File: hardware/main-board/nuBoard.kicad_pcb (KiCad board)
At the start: 6 copper layers, 141.7 x 105.1 mm, 343 parts, among them J1 FPGA Debug, J2 Barrel_Jack_Switch, J3 USB_C_Receptacle_USB2.0_16P, J4 MCU Debug, J5 Conn_01x34_Socket, J6 Conn_01x34_Socket, J7 Conn_01x34_Socket, J8 Conn_01x34_Socket, Q1 NVF5P03T3G, Q2 BSR802NL6327, SW1 MCU_Reset, SW2 MCU_Boot, U1 T120F484, U10 W25Q128JVS, U11 RP2040, U2 IS66WVH8M8BLL-100B1LI, U24 SN74LVC8T245PWR, U25 SN74LVC8T245PWR, U26 SN74LVC8T245PWR, U27 SN74LVC8T245PWR, U28 SN74LVC8T245PWR, U29 SN74LVC8T245PWR, U3 TPS2116DRL, U30 SN74LVC8T245PWR, U31 SN74LVC8T245PWR, U32 SN74LVC8T245PWR, U33 SN74LVC8T245PWR, U34 SN74LVC8T245PWR, U35 SN74LVC8T245PWR, U36 TXS0108EPW, U37 SN74LVC1T45DRL, U38 SN74LVC1T45DRL, U39 SN74LVC1T45DRL, U4 AP2112K-3.3, U40 SN74LVC1T45DRL, U41 TXS0108EPW, U5 AP2112K-3.3, U6 TPS563201, U7 TPS563201, U8 UCC27524D, U9 TPS2111APWR, Y1 50Mhz, Y2 12Mhz

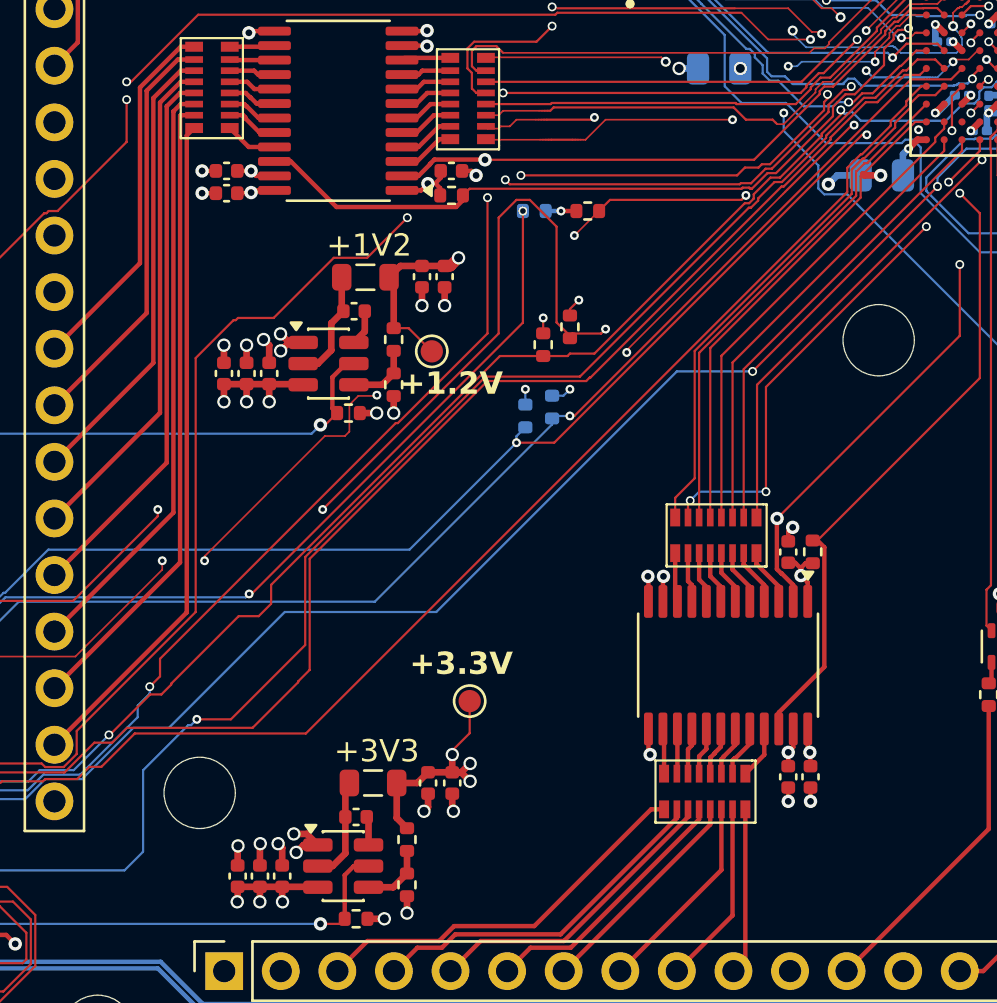
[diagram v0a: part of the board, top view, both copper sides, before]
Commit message: Fit power inductors for the FPGA buck converters
L1 and L2 used C16903, a ferrite bead, which made U6 and U7 whine and
damaged U6. Switch to C964122 in a 1008 footprint. Note that the
HyperRAM is held deselected until it is supported.

Claude-Session: https://claude.ai/code/session_01Mb721YdebqpSQrfvW2MyND
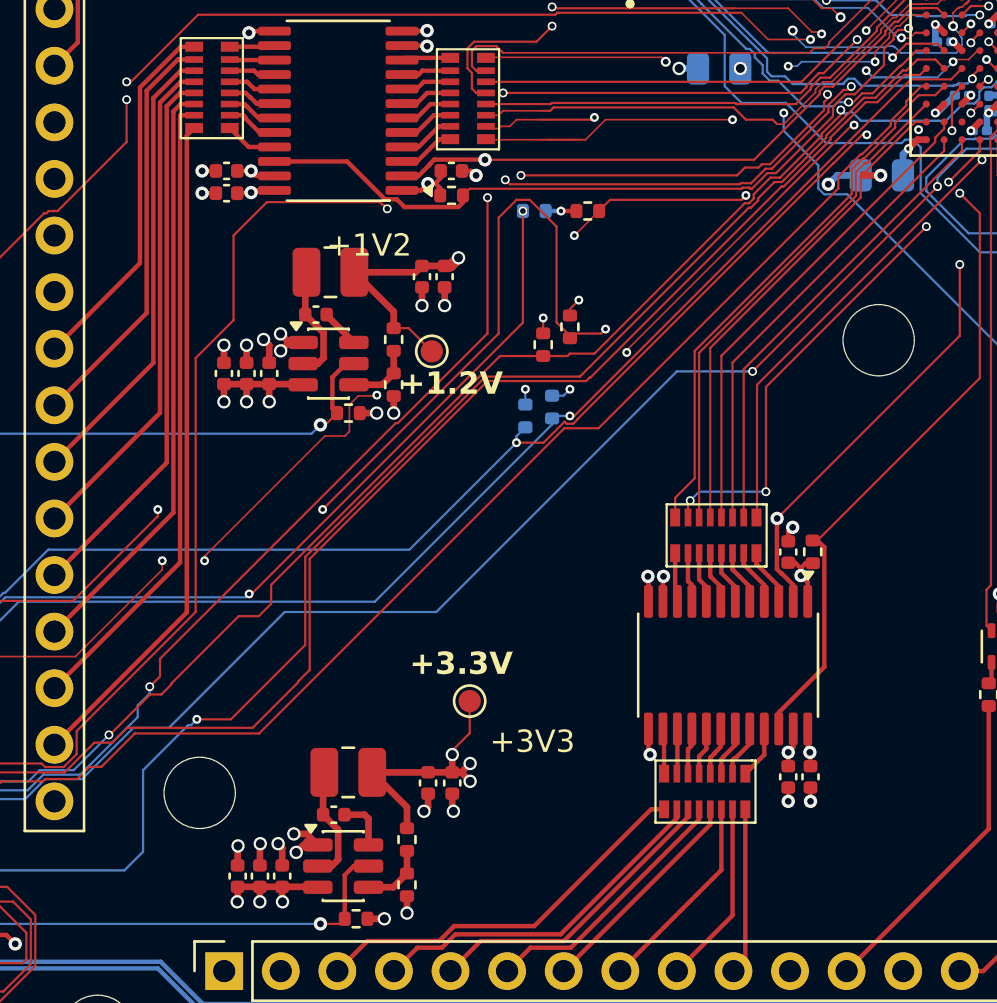
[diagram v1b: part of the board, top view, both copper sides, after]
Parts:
- L1, L2: footprint Inductor_SMD:L_0805_2012Metric -> Inductor_SMD:L_1008_2520Metric
- moved C107 1.72 mm to (72.7, 92.5)
- moved L2 1.58 mm to (73.3, 90.5)
- moved L1 1.21 mm to (74.2, 113.0)
- moved C101 1.00 mm to (73.5, 114.9)
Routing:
- net +1.2V: track 98.4 -> 100.8 mm
- net +3.3V: track 190.4 -> 192.2 mm
- net /FPGA_CSO: track 76.7 -> 78.4 mm
- net Net-(U6-VBST): track 1.29 -> 2.33 mm
- net /FPGA_CDONE: track 68.3 -> 69.1 mm
- net Net-(U7-SW): track 5.04 -> 5.82 mm
- net Net-(U6-SW): track 4.70 -> 5.36 mm
